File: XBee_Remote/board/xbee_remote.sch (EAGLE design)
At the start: 39 parts, among them IC1 AVR-MEGA8-PPTH, IC2 74LS125N, IC5 74LS595N, J1 1X2-3.5MM, J2 AVR_SPI_PRG, Y1 RESONATORPTH

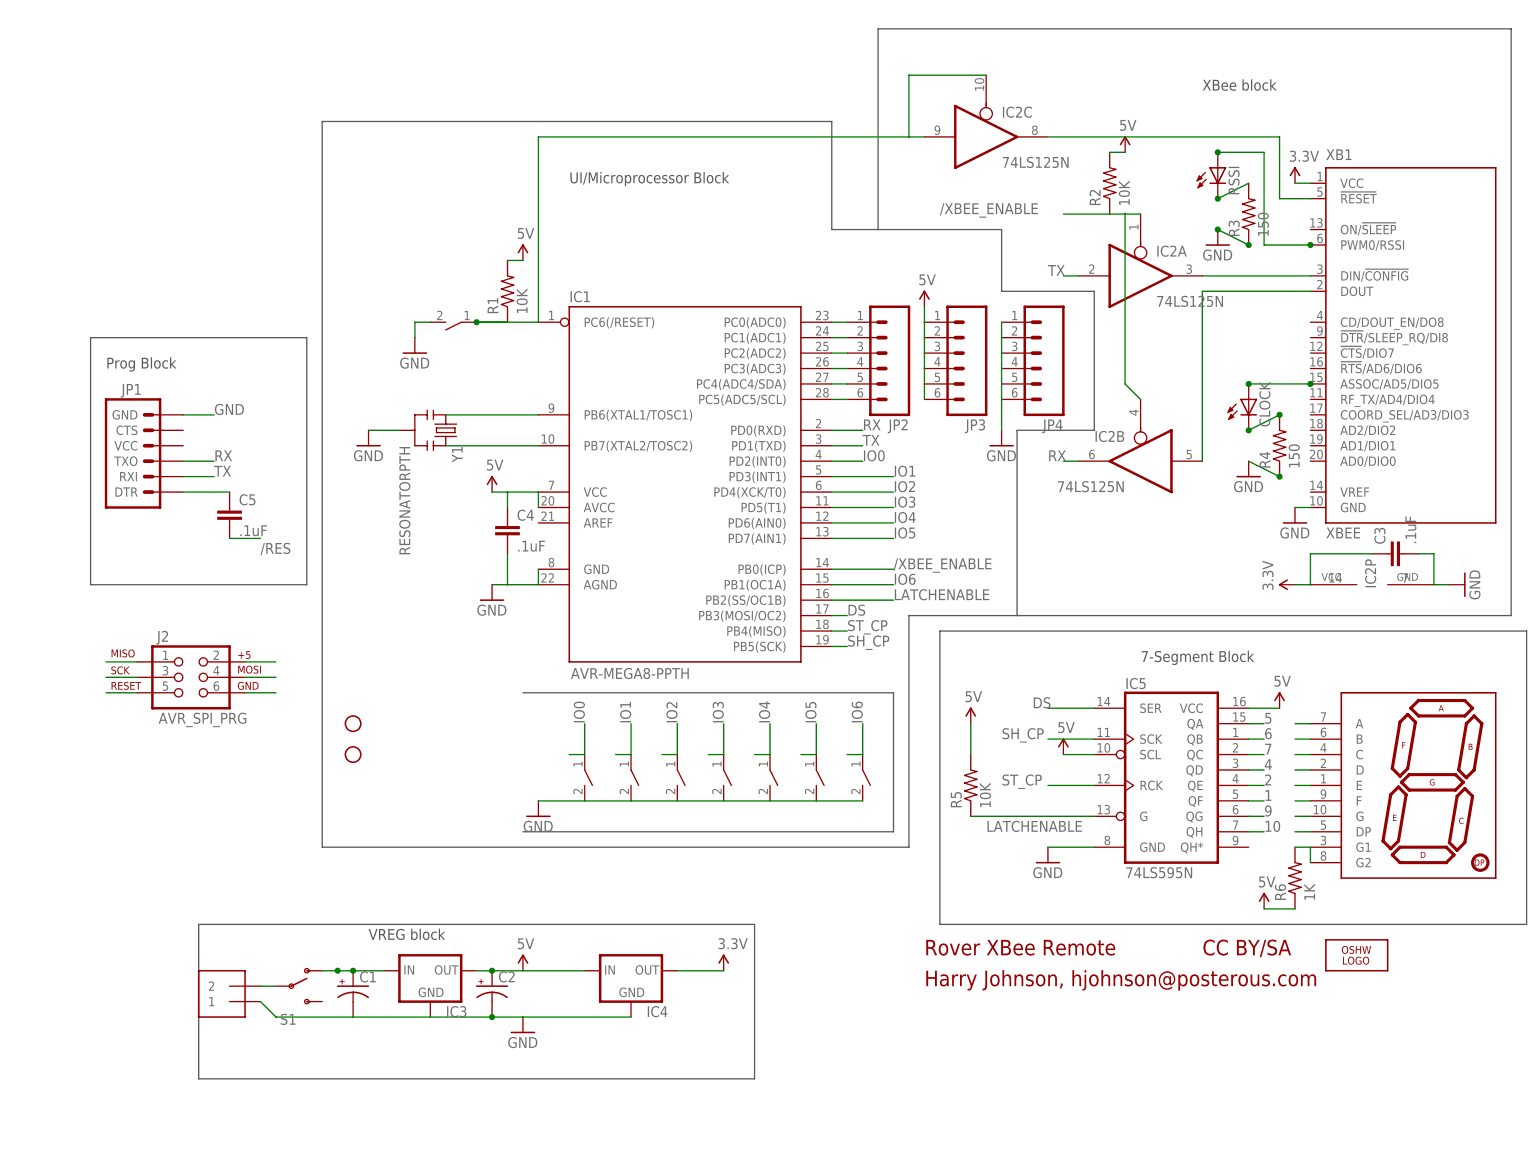
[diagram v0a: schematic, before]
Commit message: Updated through-hole board and schematic
Changed polygon fill to hatch, fully routed the board to not need
polygon, just in case, cleaned up the schematic, and added a net list
to the schematic.
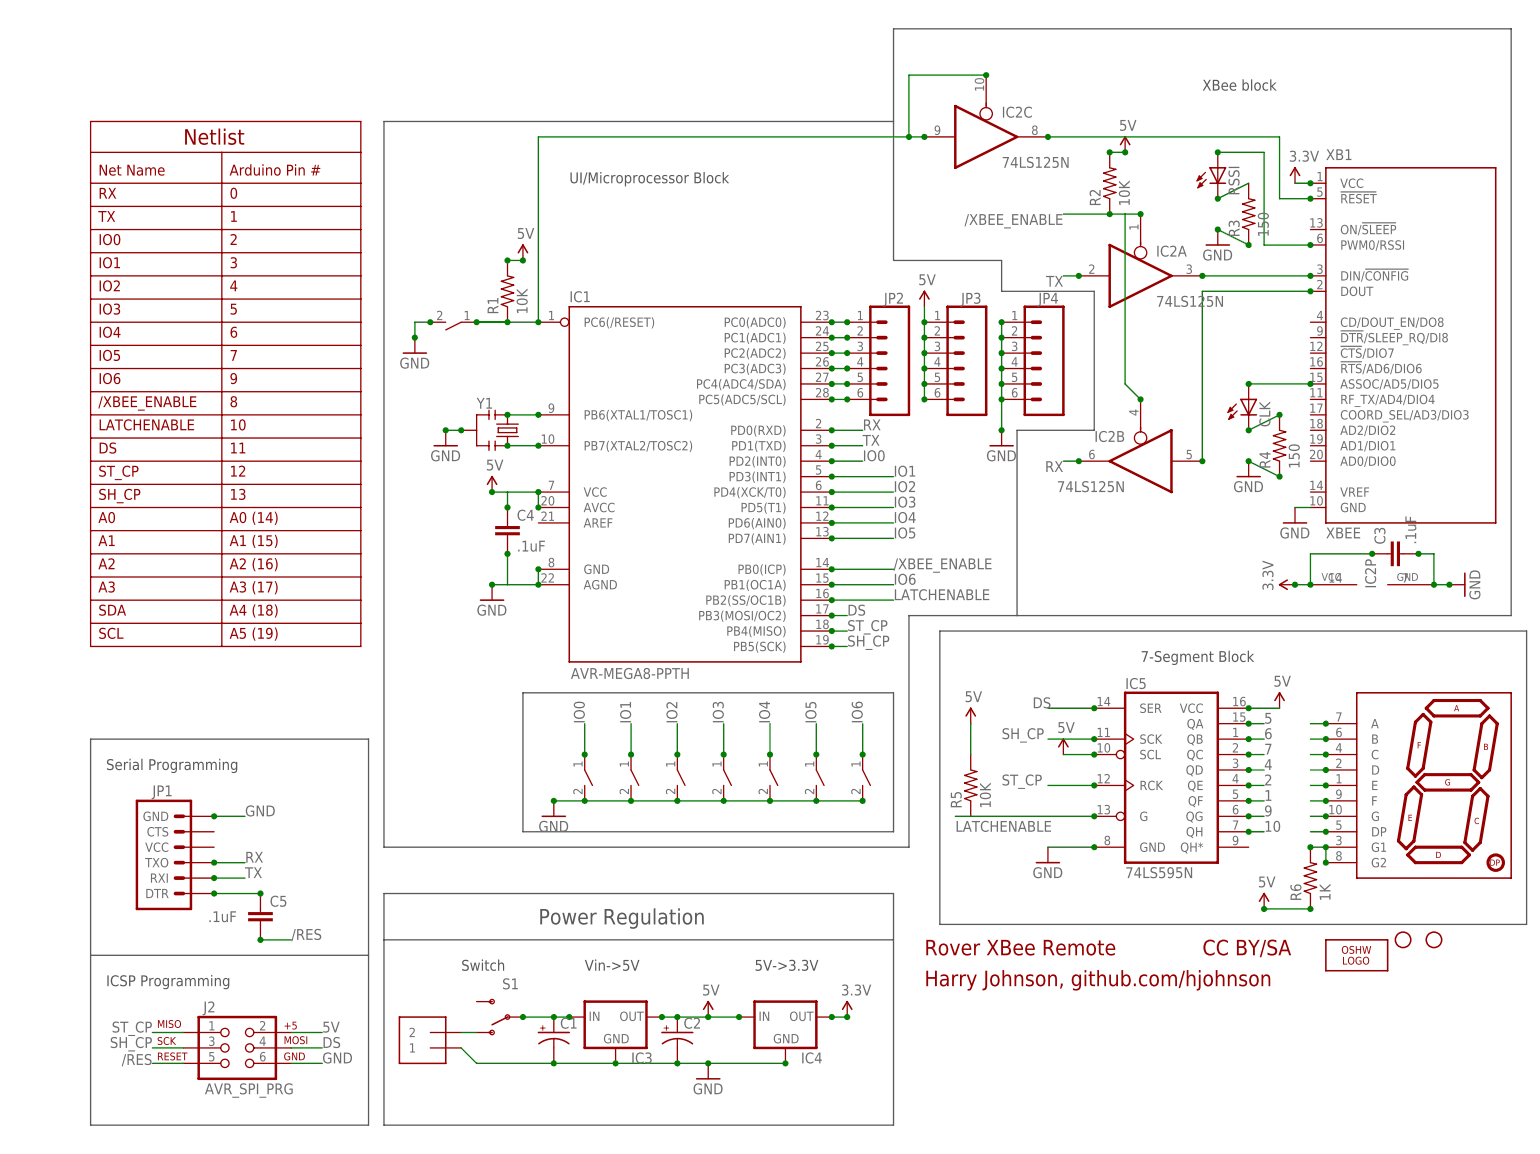
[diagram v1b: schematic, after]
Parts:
- renumbered CLOCK to CLK
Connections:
- net N$18 renamed A0
- net N$19 renamed A1
- net N$20 renamed A2
- net N$21 renamed A3
- net N$22 renamed SDA
- net N$23 renamed SCL
- removed net N$6: J1.2, S1.P
- new net N$4: J1.2, S1.O
- net N$5: now also S1.P; no longer S1.O
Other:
- note added: "/XBEE_ENABLE"
- note added: "0"
- note added: "1"
- note added: "10"
- note added: "11"
- note added: "12"
- note added: "13"
- note added: "2"
- note added: "3"
- note added: "4"
- note added: "5"
- note added: "5V->3.3V"
- note added: "6"
- note added: "7"
- note added: "8"
- note added: "9"
- note added: "A0"
- note added: "A0 (14)"
- note added: "A1"
- note added: "A1 (15)"
- note added: "A2"
- note added: "A2 (16)"
- note added: "A3"
- note added: "A3 (17)"
- note added: "A4 (18)"
- note added: "A5 (19)"
- note added: "Arduino Pin #"
- note added: "DS"
- note added: "Harry Johnson, github.com/hjohnson"
- note added: "ICSP Programming"
- note added: "IO0"
- note added: "IO1"
- note added: "IO2"
- note added: "IO3"
- note added: "IO4"
- note added: "IO5"
- note added: "IO6"
- note added: "LATCHENABLE"
- note added: "Net Name"
- note added: "Netlist"
- note added: "Power Regulation"
- note added: "RX"
- note added: "SCL"
- note added: "SDA"
- note added: "SH_CP"
- note added: "ST_CP"
- note added: "Serial Programming"
- note added: "Switch"
- note added: "TX"
- note added: "Vin->5V"
- note removed: "Harry Johnson, hjohnson@posterous.com"
- note removed: "Prog Block"
- note removed: "VREG block"
- moved on the sheet: C1, C2, C5, IC3, IC4, J2, JP1, R6, S1, Y1

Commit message: Made a bunch of changes.
Most importantly: Switched the lines for Switch 6 and XBee enable, to
make routing more sensible, and to make reading of switches take a
single for loop.
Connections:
- net /XBEE_ENABLE: now also IC1.PB1(OC1A); no longer IC1.PB0(ICP)
- net IO6: now also IC1.PB0(ICP); no longer IC1.PB1(OC1A)
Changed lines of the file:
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@@
 <text x="35.56" y="132.08" size="1.778" layer="94">6</text>
 <text x="35.56" y="128.27" size="1.778" layer="94">7</text>
-<text x="35.56" y="120.65" size="1.778" layer="94">8</text>
-<text x="35.56" y="124.46" size="1.778" layer="94">9</text>
+<text x="35.56" y="120.65" size="1.778" layer="94">9</text>
+<text x="35.56" y="124.46" size="1.778" layer="94">8</text>
 <text x="35.56" y="116.84" size="1.778" layer="94">10</text>
 <text x="35.56" y="113.03" size="1.778" layer="94">11</text>
@@
 </segment>
 <segment>
-<wire x1="134.62" y1="93.98" x2="144.78" y2="93.98" width="0.2032" layer="91"/>
-<label x="144.78" y="93.98" size="1.778" layer="95"/>
-<pinref part="IC1" gate="G$1" pin="PB0(ICP)"/>
-<junction x="134.62" y="93.98"/>
+<wire x1="134.62" y1="91.44" x2="144.78" y2="91.44" width="0.2032" layer="91"/>
+<label x="144.78" y="91.44" size="1.778" layer="95"/>
+<pinref part="IC1" gate="G$1" pin="PB1(OC1A)"/>
+<junction x="134.62" y="91.44"/>
 </segment>
 </net>
@@
 <net name="IO6" class="0">
 <segment>
-<wire x1="134.62" y1="91.44" x2="144.78" y2="91.44" width="0.2032" layer="91"/>
-<label x="144.78" y="91.44" size="1.778" layer="95"/>
-<pinref part="IC1" gate="G$1" pin="PB1(OC1A)"/>
-<junction x="134.62" y="91.44"/>
-</segment>
-<segment>
 <wire x1="139.7" y1="63.5" x2="139.7" y2="68.58" width="0.2032" layer="91"/>
 <label x="139.7" y="68.58" size="1.778" layer="95" rot="R90"/>
@@
 <junction x="139.7" y="63.5"/>
 </segment>
-</net>
+<segment>
+<wire x1="134.62" y1="93.98" x2="144.78" y2="93.98" width="0.2032" layer="91"/>
+<label x="144.78" y="93.98" size="1.778" layer="95"/>
+<pinref part="IC1" gate="G$1" pin="PB0(ICP)"/>
+<junction x="134.62" y="93.98"/>
+</segment>
+</net>

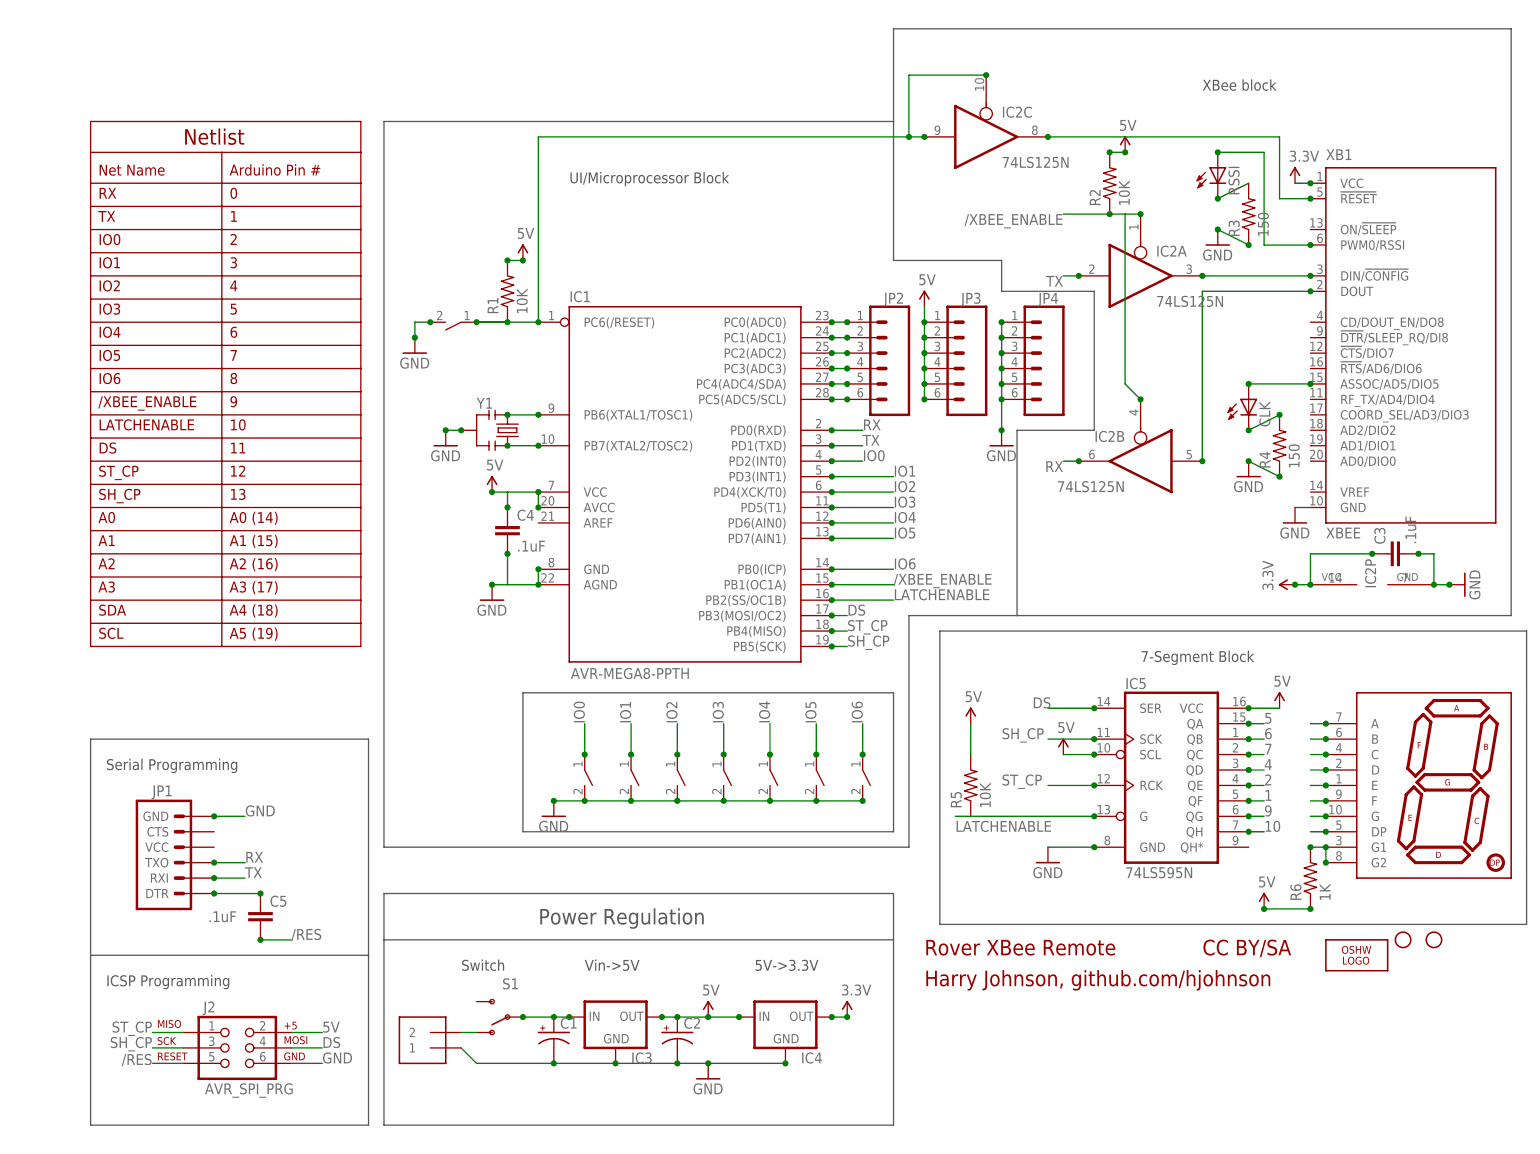
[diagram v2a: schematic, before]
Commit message: New revision of remote: Added joystick, shifted parts.
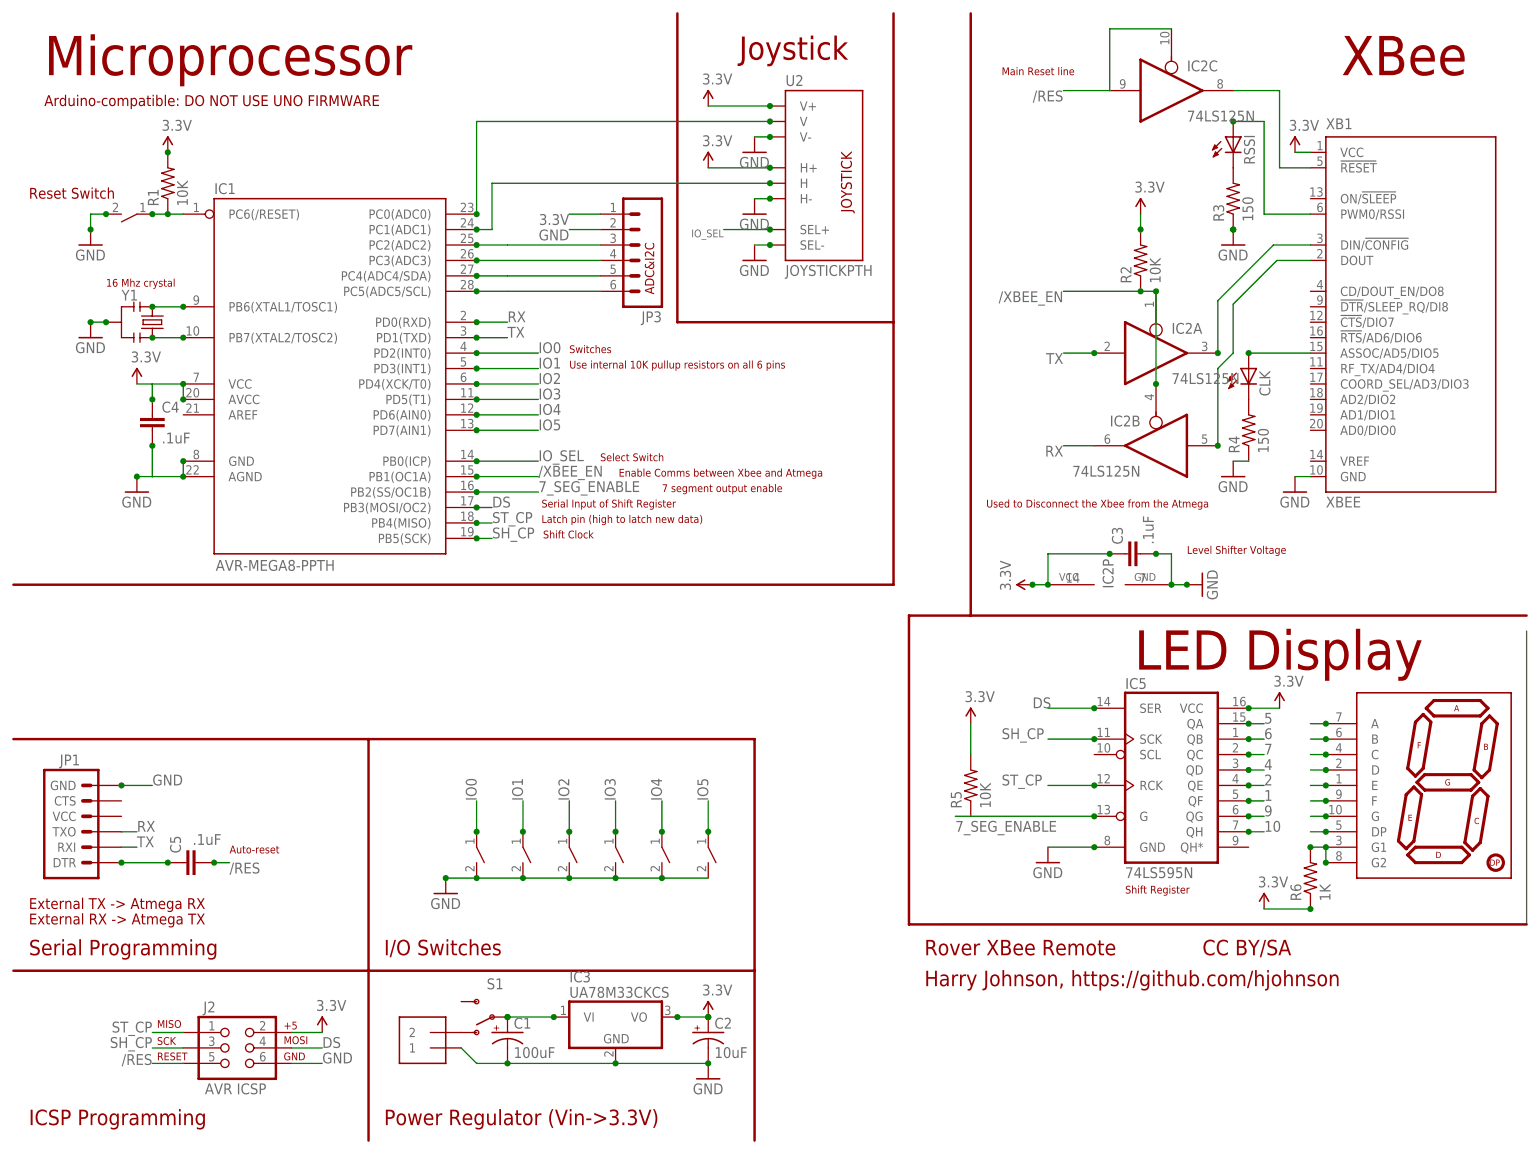
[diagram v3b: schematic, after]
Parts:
- removed IC4: (no value), adafruit:MCP1700TRI
- removed JP2, JP4: (no value), SparkFun:M06SIP
- removed JP5, JP6: STAND-OFF, SparkFun:STAND-OFF
- removed LOGO1: OSHW_LOGO_FILLX0150-NT, OSHW:OSHW_LOGO_FILLX0150-NT
- removed U$15: TACT_TL1107, customswitch:TACT_TL1107
- added U2: JOYSTICKPTH, SparkFun:JOYSTICKPTH
- C1: value (none) -> 100uF
- C2: value (none) -> 10uF
- IC3: value (none) -> UA78M33CKCS; device SparkFun:V_REG_78XXSIDE -> linear:786TV
- J2: value AVR_SPI_PRG -> AVR ICSP
- XB1: device maxstream:XBEE -> hjohnson_library:XBEE
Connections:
- net /XBEE_ENABLE renamed /XBEE_EN
- net LATCHENABLE renamed 7_SEG_ENABLE
- removed net 5V: C2.+, C4.1, IC1.AVCC, IC1.VCC@1, IC3.OUT, IC4.IN, IC5.SCL, IC5.VCC, J2.2, JP3.1, JP3.2, JP3.3, JP3.4, JP3.5, JP3.6, R1.2, R2.2, R5.2, R6.1
- removed net A0: IC1.PC0(ADC0), JP2.1
- removed net A1: IC1.PC1(ADC1), JP2.2
- removed net IO6: IC1.PB0(ICP), U$15.1
- removed net N$5: C1.+, IC3.IN, S1.P
- new net IO_SEL: IC1.PB0(ICP), U2.SEL+
- new net VIN: C1.+, IC3.VI, S1.P
- new net VIN_H: IC1.PC1(ADC1), U2.H
- new net VIN_V: IC1.PC0(ADC0), U2.V
- net 3.3V: now also C2.+, C4.1, IC1.AVCC, IC1.VCC@1, IC3.VO, IC5.VCC, J2.2, JP3.1, R1.2, R2.2, R5.2, R6.1, U2.H+, U2.V+; no longer IC4.OUT
- net A2: now also JP3.3; no longer JP2.3
- net A3: now also JP3.4; no longer JP2.4
- net GND: now also JP3.2, U2.H-, U2.SEL-, U2.V-; no longer IC4.GND, JP4.1, JP4.2, JP4.3, JP4.4, JP4.5, JP4.6, U$15.2
- net SCL: now also JP3.6; no longer JP2.6
- net SDA: now also JP3.5; no longer JP2.5
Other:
- note added: "16 Mhz crystal"
- note added: "7 segment output enable"
- note added: "ADC&I2C"
- note added: "Arduino-compatible: DO NOT USE UNO FIRMWARE"
- note added: "Auto-reset"
- note added: "Enable Comms between Xbee and Atmega"
- note added: "External RX -> Atmega TX"
- note added: "External TX -> Atmega RX"
- note added: "Harry Johnson, https://github.com/hjohnson"
- note added: "I/O Switches"
- note added: "Joystick"
- note added: "LED Display"
- note added: "Latch pin (high to latch new data)"
- note added: "Level Shifter Voltage"
- note added: "Main Reset line"
- note added: "Microprocessor"
- note added: "Power Regulator (Vin->3.3V)"
- note added: "Reset Switch"
- note added: "Select Switch"
- note added: "Serial Input of Shift Register"
- note added: "Shift Clock"
- note added: "Shift Register"
- note added: "Switches"
- note added: "Use internal 10K pullup resistors on all 6 pins"
- note added: "Used to Disconnect the Xbee from the Atmega"
- note added: "XBee"
- note removed: "/XBEE_ENABLE"
- note removed: "0"
- note removed: "1"
- note removed: "10"
- note removed: "11"
- note removed: "12"
- note removed: "13"
- note removed: "2"
- note removed: "3"
- note removed: "4"
- note removed: "5"
- note removed: "5V->3.3V"
- note removed: "6"
- note removed: "7"
- note removed: "7-Segment Block"
- note removed: "8"
- note removed: "9"
- note removed: "A0"
- note removed: "A0 (14)"
- note removed: "A1"
- note removed: "A1 (15)"
- note removed: "A2"
- note removed: "A2 (16)"
- note removed: "A3"
- note removed: "A3 (17)"
- note removed: "A4 (18)"
- note removed: "A5 (19)"
- note removed: "Arduino Pin #"
- note removed: "DS"
- note removed: "Harry Johnson, github.com/hjohnson"
- note removed: "IO0"
- note removed: "IO1"
- note removed: "IO2"
- note removed: "IO3"
- note removed: "IO4"
- note removed: "IO5"
- note removed: "IO6"
- note removed: "LATCHENABLE"
- note removed: "Net Name"
- note removed: "Netlist"
- note removed: "Power Regulation"
- note removed: "RX"
- note removed: "SCL"
- note removed: "SDA"
- note removed: "SH_CP"
- note removed: "ST_CP"
- note removed: "Switch"
- note removed: "TX"
- note removed: "UI/Microprocessor Block"
- note removed: "Vin->5V"
- note removed: "XBee block"
- moved on the sheet: C1, C2, C3, C4, C5, CLK, IC1, IC2A, IC2B, IC2C, IC2P, JP1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
